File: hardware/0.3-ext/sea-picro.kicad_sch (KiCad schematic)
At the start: 59 parts, among them J1 USB_C_Receptacle_USB2.0, J2 0.1" x 12, J3 0.1" x 12, J4 D+, J5 D-, J6 0.1" x 5, J7 2.54, Q1 2N7002VC-7, Q2 2N7002VC-7, U1 AP7365-33WG-7, U2 GD25Q64CWIGR, U3 RP2040, U4 74LVC1T45Z6-7, Y1 12MHz

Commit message: clean up routing
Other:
- title: Sea Picro Extended -> Sea Picro EXT
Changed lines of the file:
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@@
   (paper "A4")
   (title_block
-    (title "Sea Picro Extended")
-    (date "2022-03-13")
-    (rev "0.2")
+    (title "Sea Picro EXT")
+    (date "2022-06-20")
+    (rev "0.3")
     (company "Josh Johnson")
   )

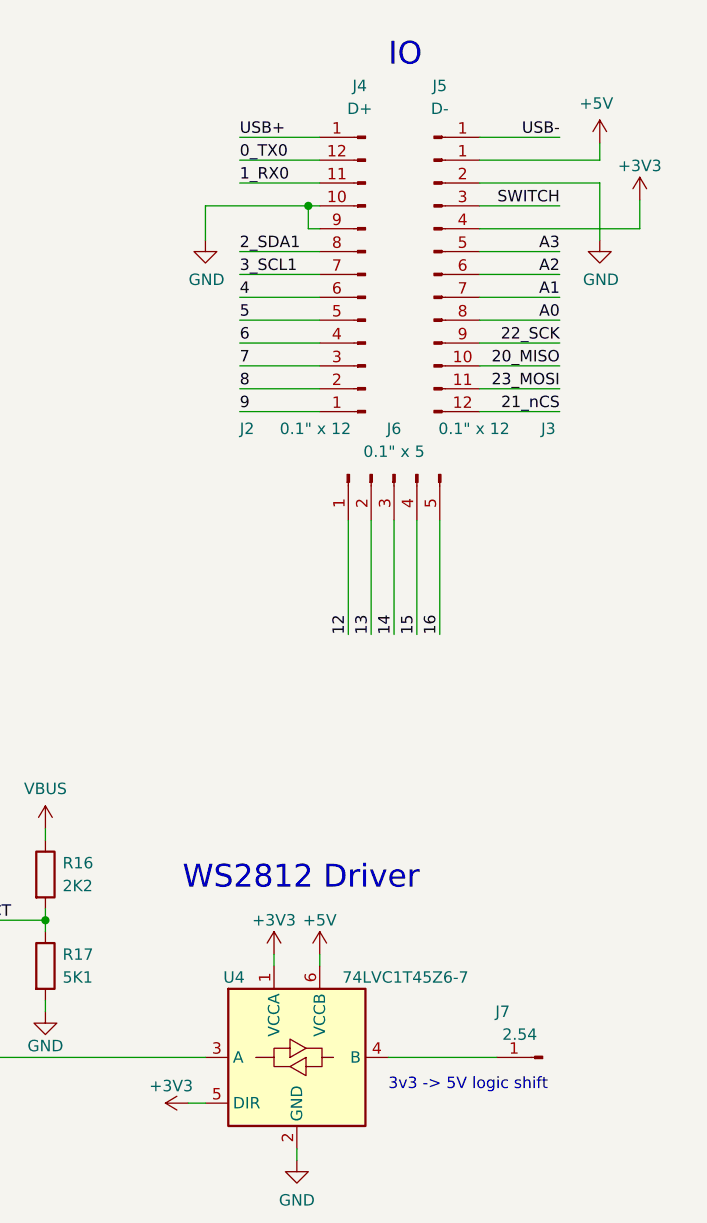
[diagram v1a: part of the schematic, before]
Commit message: sea picro footprint overhaul
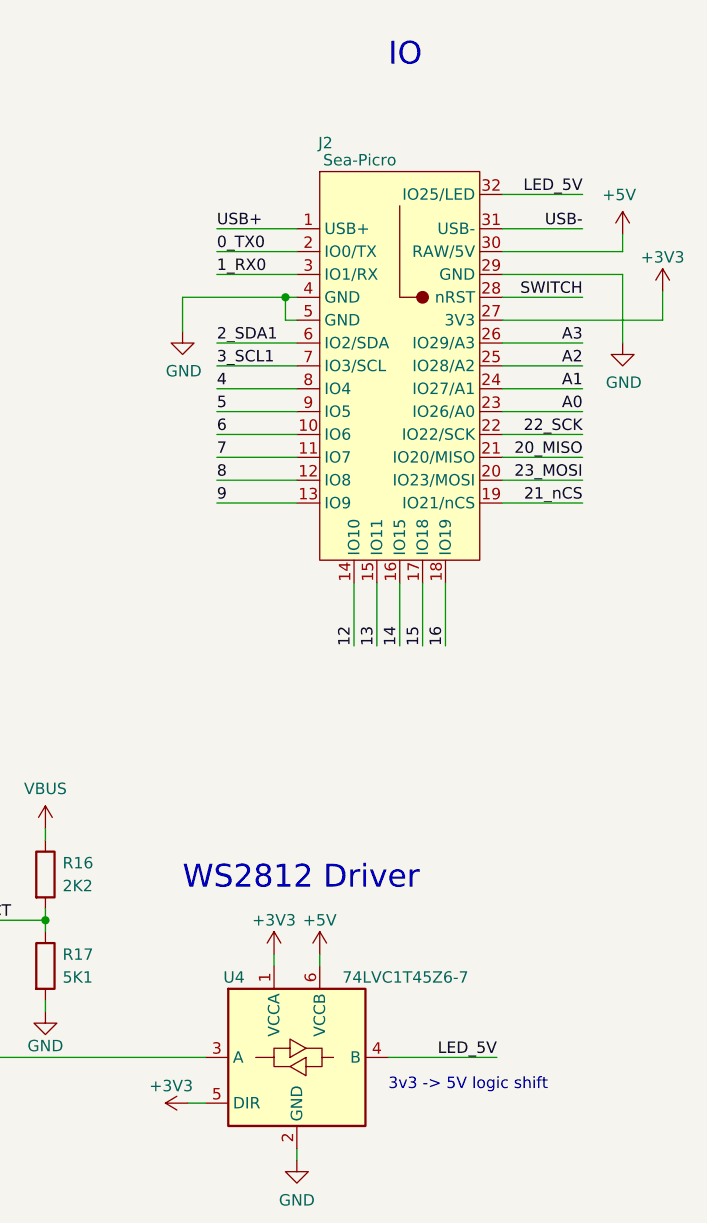
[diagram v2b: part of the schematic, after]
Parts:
- removed J2, J3: 0.1" x 12, josh-connectors:Castellated_Short_P2.54x12, symbol Connector:Conn_01x12_Male
- removed J4: D+, josh-connectors:PinHeader_1x01_P2.54mm_Circle, symbol Connector:Conn_01x01_Male
- removed J5: D-, josh-connectors:PinHeader_1x01_P2.54mm_Circle, symbol Connector:Conn_01x01_Male
- removed J6: 0.1" x 5, josh-connectors:PinHeader_1x05_P2.54mm_Circle, symbol Connector:Conn_01x05_Male
- removed J7: 2.54, josh-connectors:PinHeader_1x01_P2.54mm_Circle, symbol Connector:Conn_01x01_Male
- added J2: Sea-Picro, josh-module:Sea-Picro_EXT_Pins, symbol josh-module:Sea-Picro
- D1: footprint Diode_SMD:D_SOD-323 -> josh-passives-smt:D_SOD-323
- Q1, Q2, U4: footprint Package_TO_SOT_SMD:SOT-563 -> josh-soic-sot-etc:SOT-563
- U1: footprint Package_TO_SOT_SMD:SOT-23-5 -> josh-soic-sot-etc:SOT-23-5
- U2: footprint Package_SON:WSON-8-1EP_6x5mm_P1.27mm_EP3.4x4mm -> josh-dfn-qfn:WSON-8-1EP_6x5mm_P1.27mm_EP3.4x4mm
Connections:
- net +3V3: now also J2.27 (3V3)
- net +5V: now also J2.30 (RAW/5V)
- net 0_TX0: now also J2.2 (IO0/TX)
- net 12: now also J2.14 (IO10)
- net 13: now also J2.15 (IO11)
- net 14: now also J2.16 (IO15)
- net 15: now also J2.17 (IO18)
- net 16: now also J2.18 (IO19)
- net 1_RX0: now also J2.3 (IO1/RX)
- net 20_MISO: now also J2.21 (IO20/MISO)
- net 21_nCS: now also J2.19 (IO21/nCS)
- net 22_SCK: now also J2.22 (IO22/SCK)
- net 23_MOSI: now also J2.20 (IO23/MOSI)
- net 2_SDA1: now also J2.6 (IO2/SDA)
- net 3_SCL1: now also J2.7 (IO3/SCL)
- net 4: now also J2.8 (IO4)
- net 5: now also J2.9 (IO5)
- net 6: now also J2.10 (IO6)
- net 7: now also J2.11 (IO7)
- net 8: now also J2.12 (IO8)
- net 9: now also J2.13 (IO9)
- net A0: now also J2.23 (IO26/A0)
- net A1: now also J2.24 (IO27/A1)
- net A2: now also J2.25 (IO28/A2)
- net A3: now also J2.26 (IO29/A3)
- net GND: now also J2.29 (GND), J2.4 (GND), J2.5 (GND)
- net SWITCH: now also J2.28 (nRST)
- net USB+: now also J2.1 (USB+)
- net USB-: now also J2.31 (USB-)
- net LED_5V: now reaches U4.4 (B)
- net LED_5V: now also J2.32 (IO25/LED)

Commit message: update production outputs
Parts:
- C1, C10, C11, C12, C13, C14, C15, C16, C17, C18, C19, C2, C3, C4, C5, C6, C7, C8, C9, F1, J1, Q1, Q2, R1, R10, R11, R12, R13, R14, R15, R16, R17, R2, R3, R4, R5, R6, R7, R8, R9: Substitute (none) -> Y
- D1, U3: Substitute (none) -> N
- D2: Substitute (none) -> Y - Any Pink
- J2: now left out of the parts list
- LOGO1, LOGO2, TP1, TP2, TP3, TP4: DNP DNP -> (none)
- U1: LCSC2 (none) -> C82942; MPN2 (none) -> ME6211C33M5G-N; Manufacturer2 (none) -> MICRONE(Nanjing Micro One Elec); Substitute (none) -> Y - Confirm with Josh
- U2: LCSC2 (none) -> C2940197; MPN2 (none) -> W25Q64JVZPIQ; Manufacturer2 (none) -> Winbond; Substitute (none) -> N
- U4: value 74LVC1T45Z6-7 -> 74LVC1T45; LCSC C441819 -> C352970; MPN  74LVC1T45Z6-7 -> SN74LVC1T45DRLR; Manufacturer Diodes Incorporated -> Texas Instruments; Substitute (none) -> N
- Y1: LCSC2 (none) -> C2149205; MPN2 (none) -> 2TJ412000NYGBC; Manufacturer2 (none) -> JYJE; Substitute (none) -> N

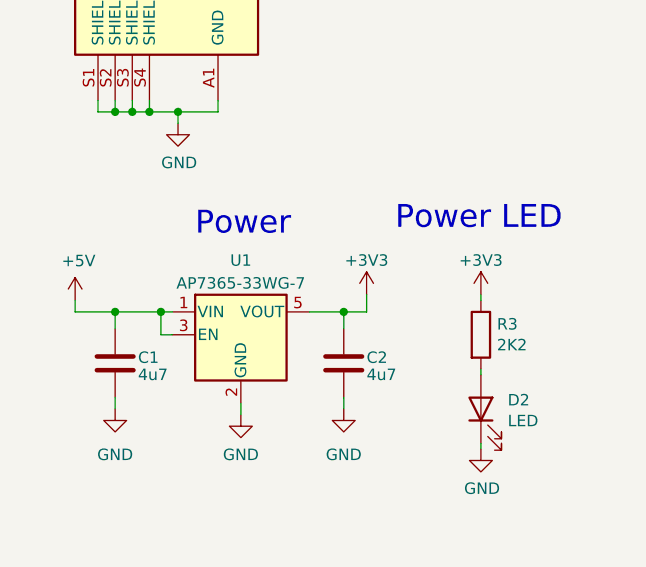
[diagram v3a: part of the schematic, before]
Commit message: add teardrops and melted versions, update LDO MPN
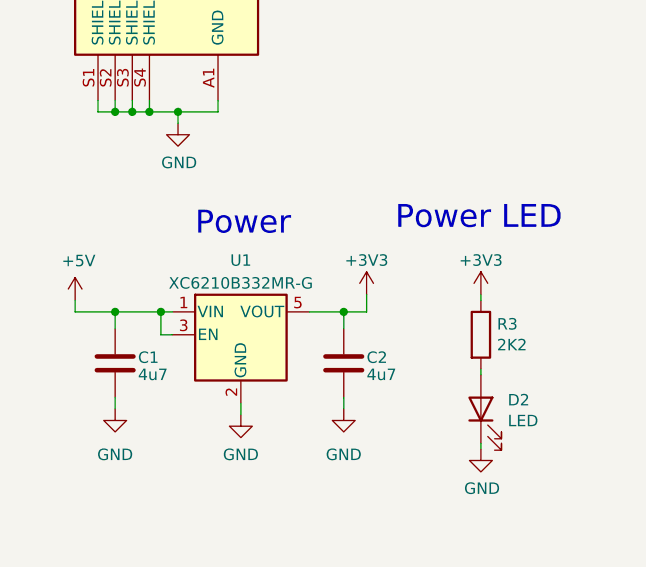
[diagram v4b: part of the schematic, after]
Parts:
- U1: value AP7365-33WG-7 -> XC6210B332MR-G; LCSC C150742 -> C47719; LCSC2 C82942 -> (none); MPN  AP7365-33WG-7 -> XC6210B332MR-G; MPN2 ME6211C33M5G-N -> (none); Manufacturer Diodes Incorporated -> Torex Semiconductor; Manufacturer2 MICRONE(Nanjing Micro One Elec) -> (none); Substitute Y - Confirm with Josh -> N
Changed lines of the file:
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@@
     (in_bom yes) (on_board yes)
     (property "Reference" "U1" (id 0) (at 42.545 86.995 0))
-    (property "Value" "AP7365-33WG-7 " (id 1) (at 42.545 89.535 0))
+    (property "Value" "XC6210B332MR-G" (id 1) (at 42.545 89.535 0))
     (property "Footprint" "josh-soic-sot-etc:SOT-23-5" (id 2) (at 42.545 86.995 0)
       (effects (font (size 1.27 1.27)) hide)
@@
       (effects (font (size 1.27 1.27)) hide)
     )
-    (property "LCSC" "C150742" (id 4) (at 42.545 95.25 0)
-      (effects (font (size 1.27 1.27)) hide)
-    )
-    (property "MPN " "AP7365-33WG-7 " (id 5) (at 42.545 95.25 0)
-      (effects (font (size 1.27 1.27)) hide)
-    )
-    (property "Manufacturer" "Diodes Incorporated" (id 6) (at 42.545 95.25 0)
+    (property "LCSC" "C47719" (id 4) (at 42.545 95.25 0)
+      (effects (font (size 1.27 1.27)) hide)
+    )
+    (property "MPN " "XC6210B332MR-G" (id 5) (at 42.545 95.25 0)
+      (effects (font (size 1.27 1.27)) hide)
+    )
+    (property "Manufacturer" "Torex Semiconductor" (id 6) (at 42.545 95.25 0)
       (effects (font (size 1.27 1.27)) hide)
     )
@@
       (effects (font (size 1.27 1.27)) hide)
     )
-    (property "MPN2" "ME6211C33M5G-N" (id 8) (at 42.545 95.25 0)
-      (effects (font (size 1.27 1.27)) hide)
-    )
-    (property "Manufacturer2" "MICRONE(Nanjing Micro One Elec) " (id 9) (at 42.545 95.25 0)
-      (effects (font (size 1.27 1.27)) hide)
-    )
-    (property "LCSC2" "C82942" (id 10) (at 42.545 95.25 0)
-      (effects (font (size 1.27 1.27)) hide)
-    )
-    (property "Substitute" "Y - Confirm with Josh" (id 11) (at 42.545 95.25 0)
+    (property "MPN2" "" (id 8) (at 42.545 95.25 0)
+      (effects (font (size 1.27 1.27)) hide)
+    )
+    (property "Manufacturer2" "" (id 9) (at 42.545 95.25 0)
+      (effects (font (size 1.27 1.27)) hide)
+    )
+    (property "LCSC2" "" (id 10) (at 42.545 95.25 0)
+      (effects (font (size 1.27 1.27)) hide)
+    )
+    (property "Substitute" "N" (id 11) (at 42.545 95.25 0)
       (effects (font (size 1.27 1.27)) hide)
     )
@@
     )
     (path "/d26fce45-c1d6-42bc-931d-972bf3799097"
-      (reference "U1") (unit 1) (value "AP7365-33WG-7 ") (footprint "josh-soic-sot-etc:SOT-23-5")
+      (reference "U1") (unit 1) (value "XC6210B332MR-G") (footprint "josh-soic-sot-etc:SOT-23-5")
     )
     (path "/578f7d98-6025-491f-b2c7-18b0b10fb26e"

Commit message: fix 1u cap bom
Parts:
- C12, C9: LCSC C15849 -> C52923; MPN  CL10A105KB8NNNC -> CL05A105KA5NQNC
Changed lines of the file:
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@@
       (effects (font (size 1.27 1.27)) hide)
     )
-    (property "LCSC" "C15849" (id 4) (at 131.445 74.93 0)
-      (effects (font (size 1.27 1.27)) hide)
-    )
-    (property "MPN " "CL10A105KB8NNNC" (id 5) (at 131.445 74.93 0)
+    (property "LCSC" "C52923" (id 4) (at 131.445 74.93 0)
+      (effects (font (size 1.27 1.27)) hide)
+    )
+    (property "MPN " "CL05A105KA5NQNC" (id 5) (at 131.445 74.93 0)
       (effects (font (size 1.27 1.27)) hide)
     )
@@
       (effects (font (size 1.27 1.27)) hide)
     )
-    (property "LCSC" "C15849" (id 4) (at 138.43 60.96 0)
-      (effects (font (size 1.27 1.27)) hide)
-    )
-    (property "MPN " "CL10A105KB8NNNC" (id 5) (at 138.43 60.96 0)
-      (effects (font (size 1.27 1.27)) hide)
-    )
+    (property "LCSC" "C52923" (id 4) (at 138.43 60.96 0)
+      (effects (font (size 1.27 1.27)) hide)
+    )
+    (property "MPN " "CL05A105KA5NQNC" (id 5) (at 138.43 60.96 0)
+      (effects (font (size 1.27 1.27)) hide)
+    )
